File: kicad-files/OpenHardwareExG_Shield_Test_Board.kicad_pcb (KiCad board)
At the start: 4 copper layers, 147.3 x 81.3 mm, 137 parts, among them P1 CONN_1, P11 CONN_1, P12 CONN_1, P13 CONN_1, P14 CONN_1, P15 CONN_1, P16 CONN_1, P17 CONN_1, P18 CONN_1, P19 ARDUINO_SHIELD, P2 CONN_1, P23 CONN_1, P24 CONN_1, P25 CONN_1, P26 CONN_1, P27 CONN_1, P28 CONN_1, P29 CONN_1, P3 CONN_1, P30 CONN_1, P31 CONN_1, P32 CONN_1, P33 CONN_1, P34 CONN_1, P35 CONN_1, P36 CONN_1, P37 CONN_1, P38 CONN_1, P39 CONN_1, P4 CONN_1, P40 CONN_1, P41 CONN_1, P42 CONN_1, P43 CONN_1, P44 CONN_1, P45 CONN_1, P46 CONN_1, P47 CONN_1, P48 CONN_1, P49 CONN_1, P5 CONN_1, P50 CONN_1, P51 CONN_1, P52 CONN_1, P53 CONN_1, P54 CONN_1, P55 CONN_1, P56 CONN_3X2, P57 CONN_20X2, P6 CONN_1, P7 CONN_1, P8 CONN_1, P9 CONN_1, SW1 SW_PUSH, U1 74HC165, U2 74HC165, U3 74HC595PWR, U4 74HC165, U5 74LS125, U6 TPS2095D, U8 SI8661

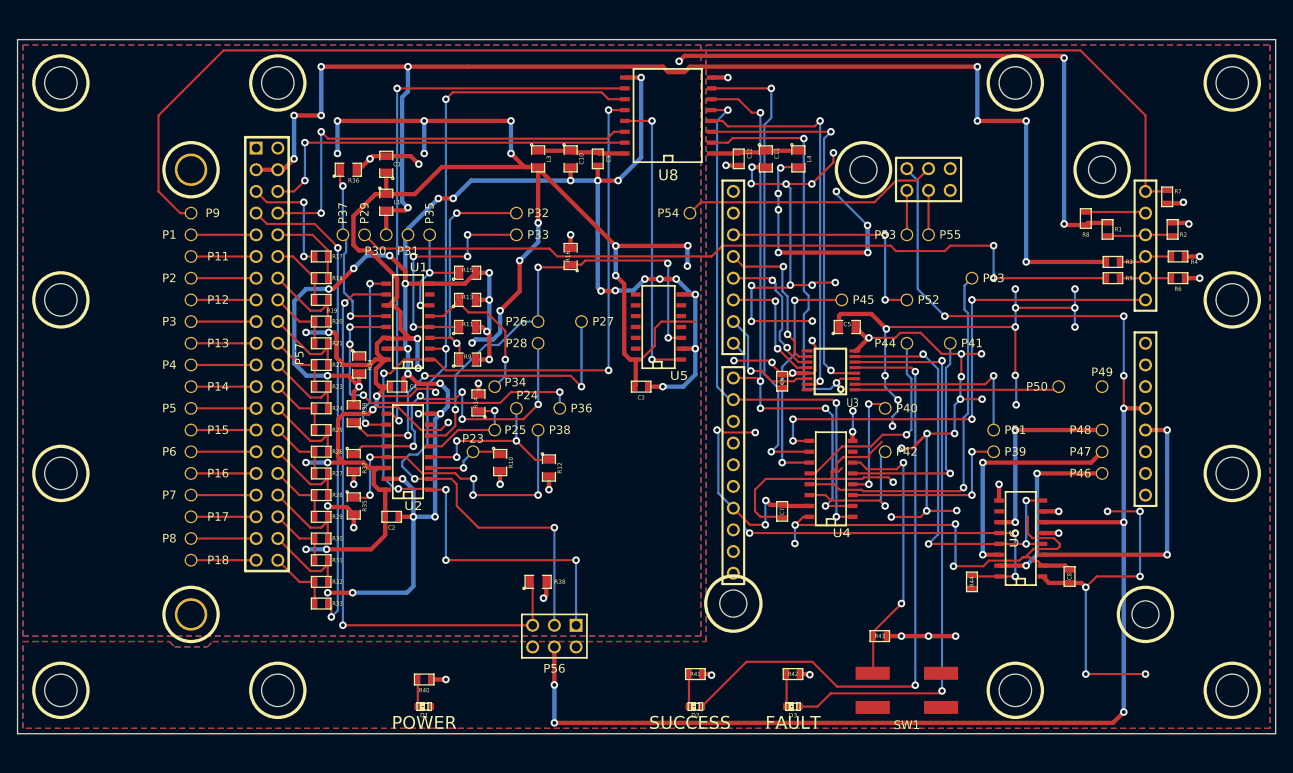
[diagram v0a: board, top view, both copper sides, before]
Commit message: finish labels on test board
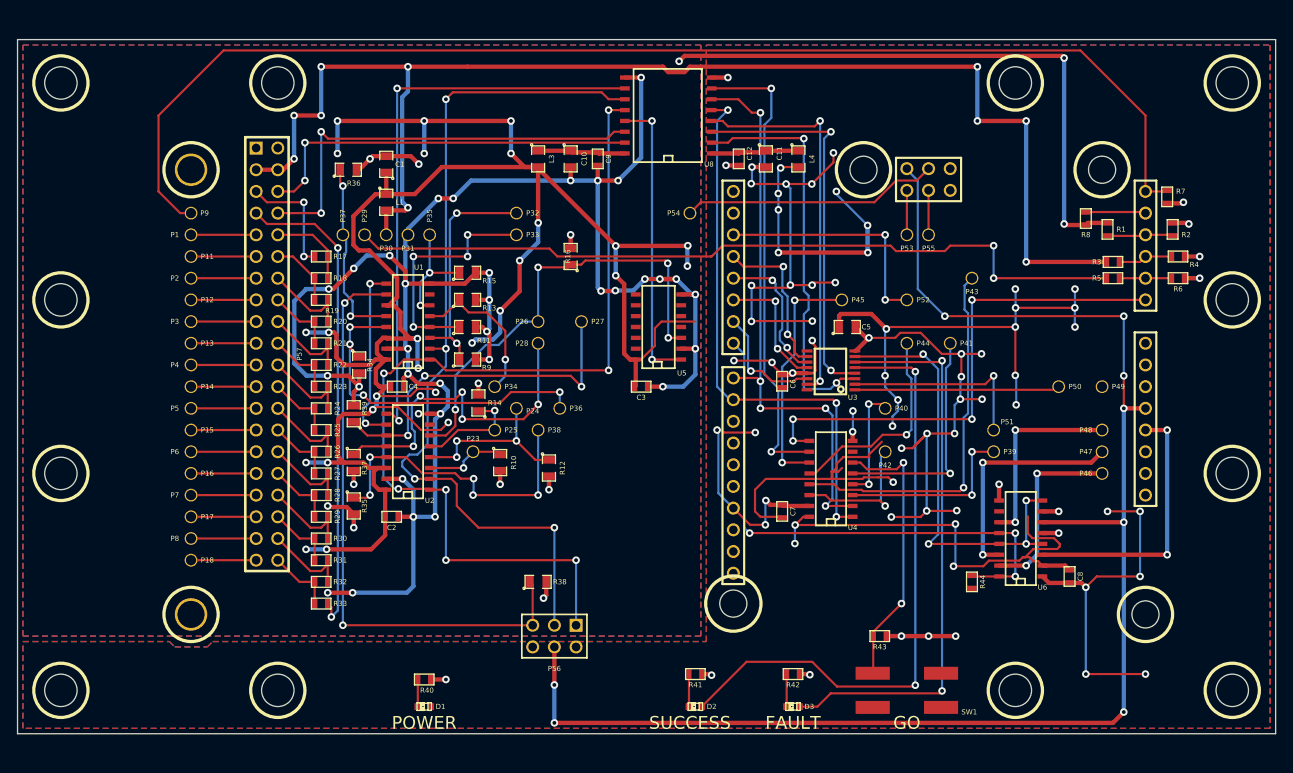
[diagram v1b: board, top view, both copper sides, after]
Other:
- board text added: "GO"

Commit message: add addition text and CERN OHL logos (on copper layer, too)
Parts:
- added G***: LOGO, LOGO, F.Cu at (124.5, 84.5)
- added G***: LOGO, LOGO, F.Cu at (63.5, 80.0)
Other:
- board text added: "CERN Open Hardware License v1.2"
- board text added: "OpenHardwareExG_Shield Test Harness v0.0 Ace Medlock Eric Herman Kendrick Shaw"
- board text added: "http://openelectronicslab.github.io/OpenHardwareExG_Shield/"
